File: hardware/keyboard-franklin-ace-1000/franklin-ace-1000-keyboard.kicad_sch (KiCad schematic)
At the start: 156 parts, among them J1 Conn_02x20_Odd_Even, K1 ESC, K10 A, K11 Z, K12 2 @, K13 W, K14 S, K15 X, K16 3 #, K17 E, K18 D, K19 C, K2 BREAK, K20 4 $, K21 R, K22 F, K23 V, K24 5 &, K25 T, K26 G, K27 B, K28 6 ^, K29 Y, K3 PAUSE, K30 H, K31 N, K32 SPACE, K33 7 &, K34 U, K35 J, K36 M, K37 8 *, K38 I, K39 K, K4 CTRL, K40 , <, K41 9 (, K42 O, K43 L, K44 . >, K45 RIGHT, K46 -, K47 +, K48 *, K49 0 ), K5 TAB, K50 P, K51 ; :, K52 / ?, K53 7, K54 4, K55 1, K56 >, K57 - / _, K58 [ {, K59 ; ", K6 LOCK, K60 SHIFT, K61 8, K62 5, K63 2, K64 0, K65 + / =, K66 ] }, K67 RETURN, K68 LEFT, K69 9, K7 SHIFT, K70 6, K71 3, K72 ., K8 1 !, K9 Q

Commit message: More work on diode-per-keyboard
extend spacebar to 9u
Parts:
- added D83: diode-combined, unikbd:diode-combined, symbol unikbd:diode-combined
- added K73: SPACE_1U, unikbd:Key_MX, symbol Connector:Conn_01x02_Pin
- K1, K10, K11, K12, K13, K14, K15, K16, K17, K18, K19, K2, K20, K21, K22, K23, K24, K25, K26, K27, K28, K29, K3, K30, K31, K33, K34, K35, K36, K37, K38, K39, K4, K40, K41, K42, K43, K44, K45, K46, K47, K48, K49, K50, K51, K52, K53, K54, K55, K56, K57, K58, K59, K6, K61, K62, K63, K64, K65, K66, K69, K70, K71, K72, K8, K9: footprint Button_Switch_Keyboard:SW_Cherry_MX_1.00u_Plate -> unikbd:Key_MX
- K32: value SPACE -> SPACE_8U; footprint Button_Switch_Keyboard:SW_Cherry_MX_6.25u_PCB -> unikbd:Key_MX_Spacebar_5.25
- K5, K67: footprint Button_Switch_Keyboard:SW_Cherry_MX_1.50u_Plate -> unikbd:Key_MX
- K60: footprint Button_Switch_Keyboard:SW_Cherry_MX_2.00u_Plate -> unikbd:Key_MX_2u
- K68: footprint Button_Switch_Keyboard:SW_Cherry_MX_1.25u_Plate -> unikbd:Key_MX
- K7: footprint Button_Switch_Keyboard:SW_Cherry_MX_2.25u_Plate -> unikbd:Key_MX_2u
- renumbered D10 to D73, D9 to D74, D1 to D75, D2 to D76, D3 to D77, D4 to D78, D5 to D79, D6 to D80, D7 to D81, D8 to D82
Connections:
- net Col0: now also K1.1 (Pin_1), K16.1 (Pin_1), K24.1 (Pin_1), K33.1 (Pin_1), K41.1 (Pin_1), K49.1 (Pin_1), K57.1 (Pin_1), K65.1 (Pin_1), K8.1 (Pin_1), K73.1 (Pin_1); no longer D1.2 (A), D10.2 (A), D11.2 (A), D12.2 (A), D13.2 (A), D14.2 (A), D15.2 (A), D16.2 (A), D17.2 (A), D18.2 (A), D19.2 (A), D2.2 (A), D20.2 (A), D21.2 (A), D22.2 (A), D23.2 (A), D24.2 (A), D25.2 (A), D26.2 (A), D27.2 (A), D28.2 (A), D29.2 (A), D3.2 (A), D30.2 (A), D31.2 (A), D32.2 (A), D33.2 (A), D34.2 (A), D35.2 (A), D36.2 (A), D37.2 (A), D38.2 (A), D39.2 (A), D4.2 (A), D40.2 (A), D41.2 (A), D42.2 (A), D43.2 (A), D44.2 (A), D45.2 (A), D46.2 (A), D47.2 (A), D48.2 (A), D49.2 (A), D5.2 (A), D50.2 (A), D51.2 (A), D52.2 (A), D53.2 (A), D54.2 (A), D55.2 (A), D56.2 (A), D57.2 (A), D58.2 (A), D59.2 (A), D6.2 (A), D60.2 (A), D61.2 (A), D62.2 (A), D63.2 (A), D64.2 (A), D65.2 (A), D66.2 (A), D67.2 (A), D68.2 (A), D69.2 (A), D7.2 (A), D70.2 (A), D71.2 (A), D72.2 (A), D75.2 (A), D76.2 (A), D77.2 (A), D78.2 (A), D79.2 (A), D8.2 (A), D80.2 (A), D81.2 (A), D82.2 (A), D9.2 (A)
- net Col1: now also K17.1 (Pin_1), K2.1 (Pin_1), K25.1 (Pin_1), K34.1 (Pin_1), K42.1 (Pin_1), K50.1 (Pin_1), K58.1 (Pin_1), K66.1 (Pin_1), K9.1 (Pin_1)
- net Col3: now also K52.1 (Pin_1)
- net Row9: now also D65.2 (A), D66.2 (A), D67.2 (A), D68.2 (A), D69.2 (A), D70.2 (A), D71.2 (A), D72.2 (A)
- new net: D83.1 (K), K73.2 (Pin_2)
- new net Row0: D1.2 (A), D2.2 (A), D3.2 (A), D32.2 (A), D4.2 (A), D5.2 (A), D6.2 (A), D7.2 (A), D82.2 (A)
- new net Row1: D10.2 (A), D11.2 (A), D12.2 (A), D13.2 (A), D14.2 (A), D15.2 (A), D8.2 (A), D81.2 (A), D9.2 (A)
- new net Row10: D83.2 (A)
- new net Row2: D16.2 (A), D17.2 (A), D18.2 (A), D19.2 (A), D20.2 (A), D21.2 (A), D22.2 (A), D23.2 (A), D80.2 (A)
- new net Row3: D24.2 (A), D25.2 (A), D26.2 (A), D27.2 (A), D28.2 (A), D29.2 (A), D30.2 (A), D31.2 (A), D79.2 (A)
- new net Row4: D33.2 (A), D34.2 (A), D35.2 (A), D36.2 (A), D37.2 (A), D38.2 (A), D39.2 (A), D40.2 (A), D78.2 (A)
- new net Row5: D41.2 (A), D42.2 (A), D43.2 (A), D44.2 (A), D45.2 (A), D46.2 (A), D47.2 (A), D48.2 (A), D77.2 (A)
- new net Row6: D49.2 (A), D50.2 (A), D51.2 (A), D52.2 (A), D53.2 (A), D54.2 (A), D55.2 (A), D56.2 (A), D76.2 (A)
- new net Row7: D57.2 (A), D58.2 (A), D59.2 (A), D60.2 (A), D61.2 (A), D62.2 (A), D63.2 (A), D64.2 (A), D75.2 (A)

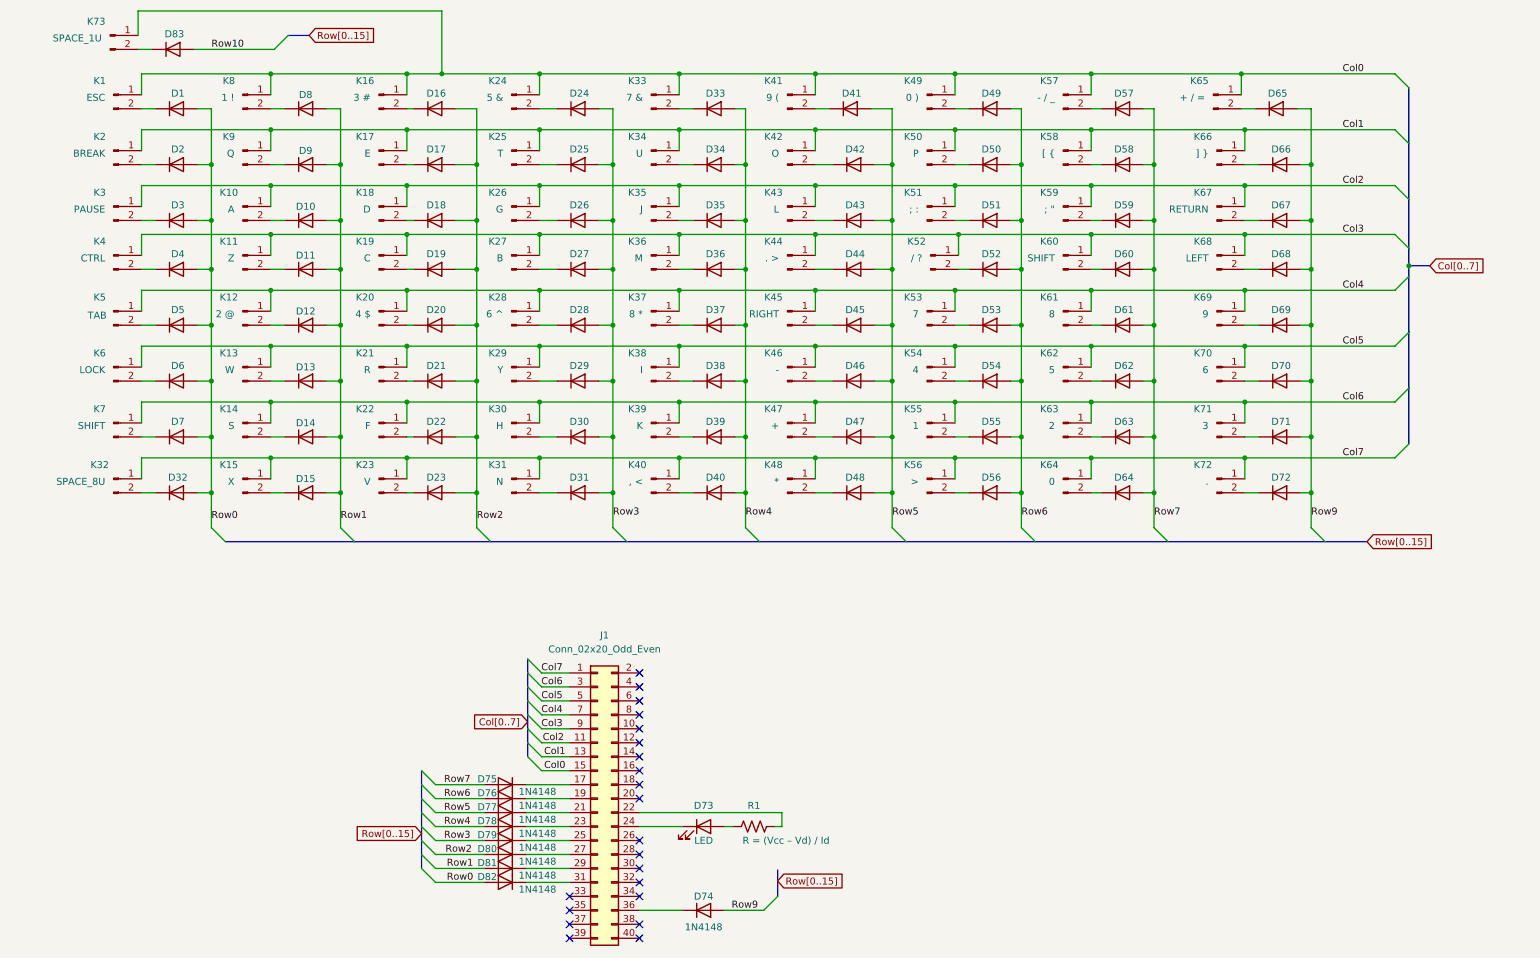
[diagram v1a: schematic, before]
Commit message: Updates to Franklin Ace keyboard
- Use the dual footprints for futaba / cherry keys

- include a diode for every key.

- Add stabilizers to the spacebar

- The Franklin keyboard is 9u, but it's very hard to find a 9u option. Instead, use 8u+1u

- Replace the LOCK key with a 1.75U key with LED window. Fix LED spacing to match original.
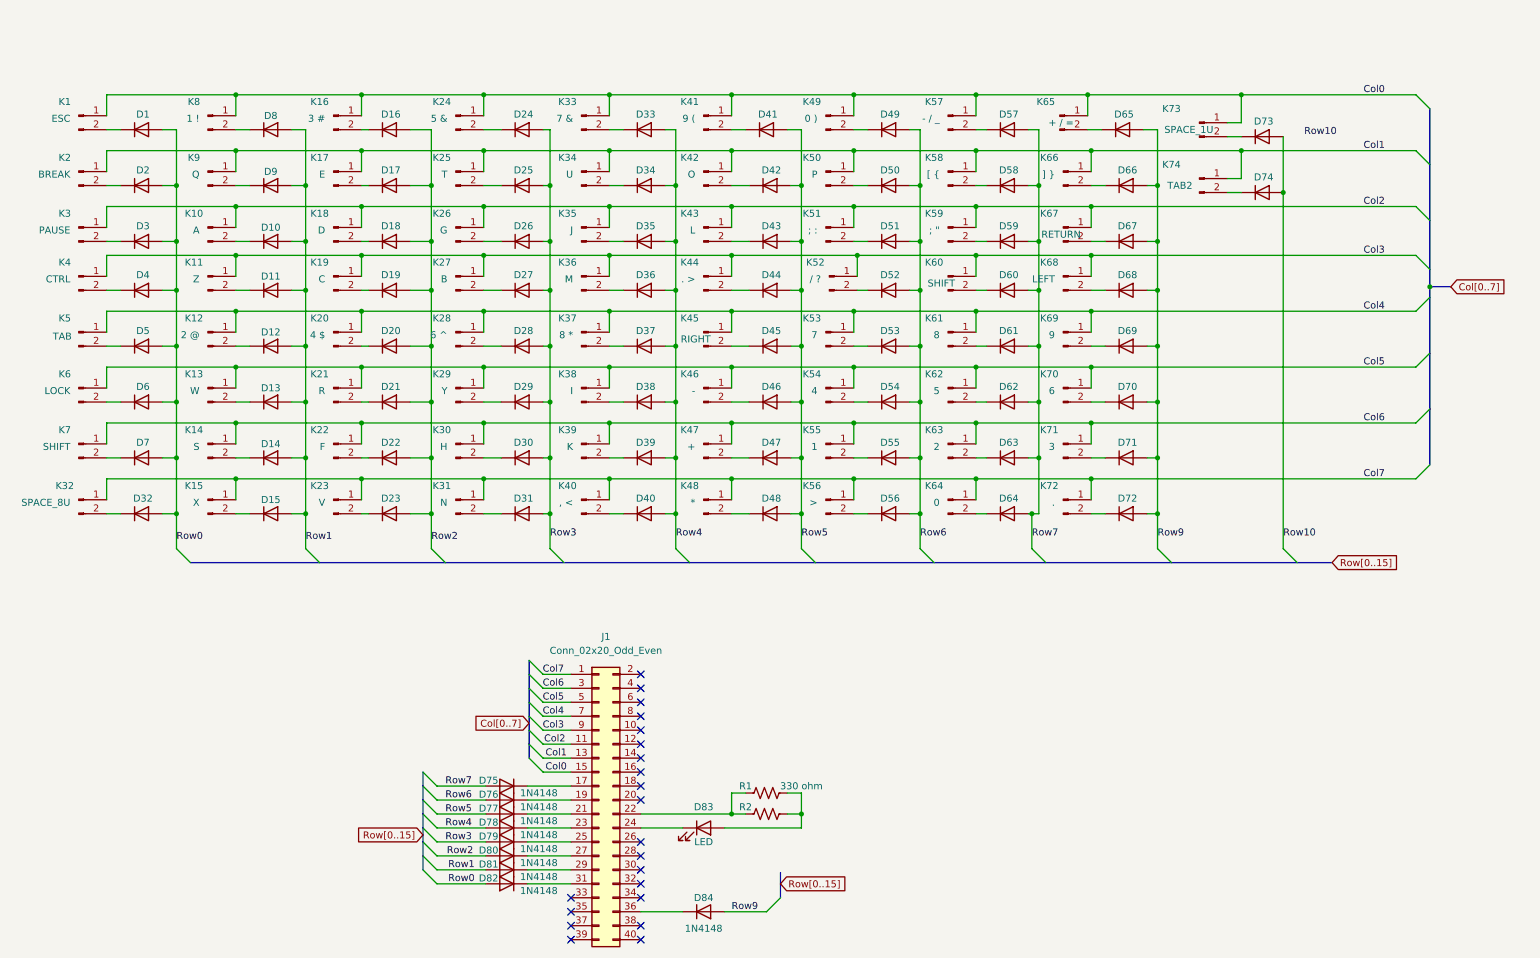
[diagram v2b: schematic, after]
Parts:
- removed R1: R = (Vcc – Vd) / Id, Resistor_THT:R_Axial_DIN0207_L6.3mm_D2.5mm_P7.62mm_Horizontal, symbol Device:R_US
- added D74: diode-combined, unikbd:diode-combined, symbol unikbd:diode-combined
- added K74: TAB2, unikbd:Key_MX, symbol Connector:Conn_01x02_Pin
- added R1: 330 ohms, Resistor_THT:R_Axial_DIN0207_L6.3mm_D2.5mm_P7.62mm_Horizontal, symbol unikbd:RES 330 ohm 1% metal film.Yageo
- added R2: RES 330 ohm 1% MLCC 0805 Yageo, Resistor_SMD:R_0805_2012Metric, symbol unikbd:RES 330 ohm 1% MLCC 0805 Yageo
- D75, D76, D77, D78, D79, D80, D81, D82: footprint Diode_THT:D_DO-35_SOD27_P7.62mm_Horizontal -> unikbd:diode-combined
- D84: renamed from D74; footprint Diode_THT:D_DO-35_SOD27_P7.62mm_Horizontal -> unikbd:diode-combined
- renumbered D83 to D73, D73 to D83
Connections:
- net Col1: now also K74.1 (Pin_1)
- net Row10: now also D74.2 (A)
- net at J1.22 (Pin_22): now also R1.2, R2.2
- net at D83.2 (A): now also R1.1, R2.1
- new net: D74.1 (K), K74.2 (Pin_2)
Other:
- moved on the sheet: D1, D10, D11, D12, D13, D14, D15, D16, D17, D18, D19, D2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

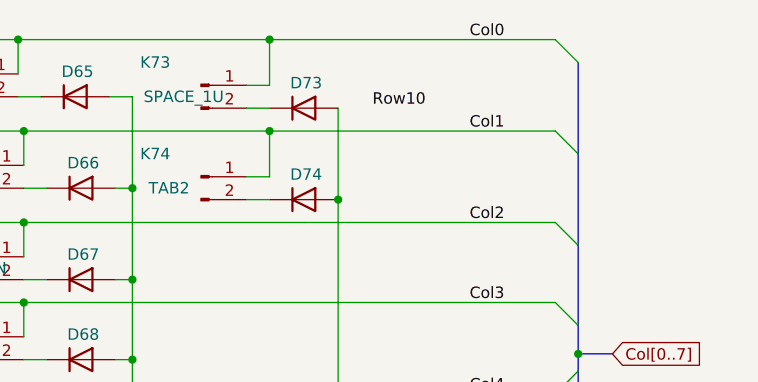
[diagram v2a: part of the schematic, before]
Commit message: Update the keyboard to use project conventions
- Use the dual footprints for futaba / cherry keys
- Include a diode for every key (dual SMT/TH options)
- Add stabilizers to the spacebar
- Add cherry and futaba aligner plates
- Add SMT resistor option
- Add unified retro keyboard text
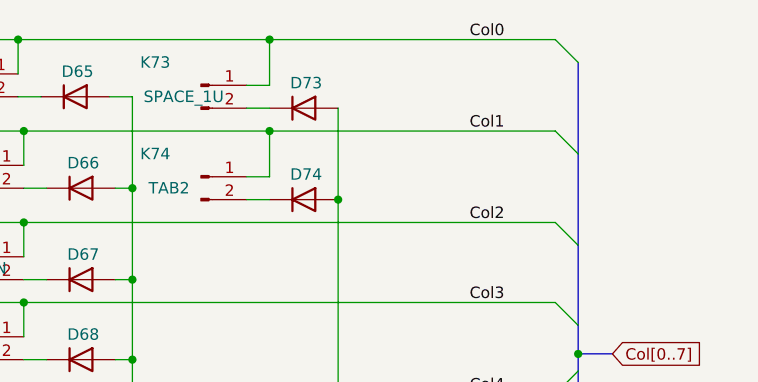
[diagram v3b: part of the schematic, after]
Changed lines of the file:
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@@
     (stroke (width 0) (type default))
-  )
-  (label "Row10" (at 246.38 41.91 0) (fields_autoplaced)
-    (effects (font (size 1.27 1.27)) (justify left bottom))
   )
   (label "Col4" (at 111.76 147.32 180) (fields_autoplaced)
